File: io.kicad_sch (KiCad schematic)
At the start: 6 parts, among them J1 SM03B-SRSS-TB

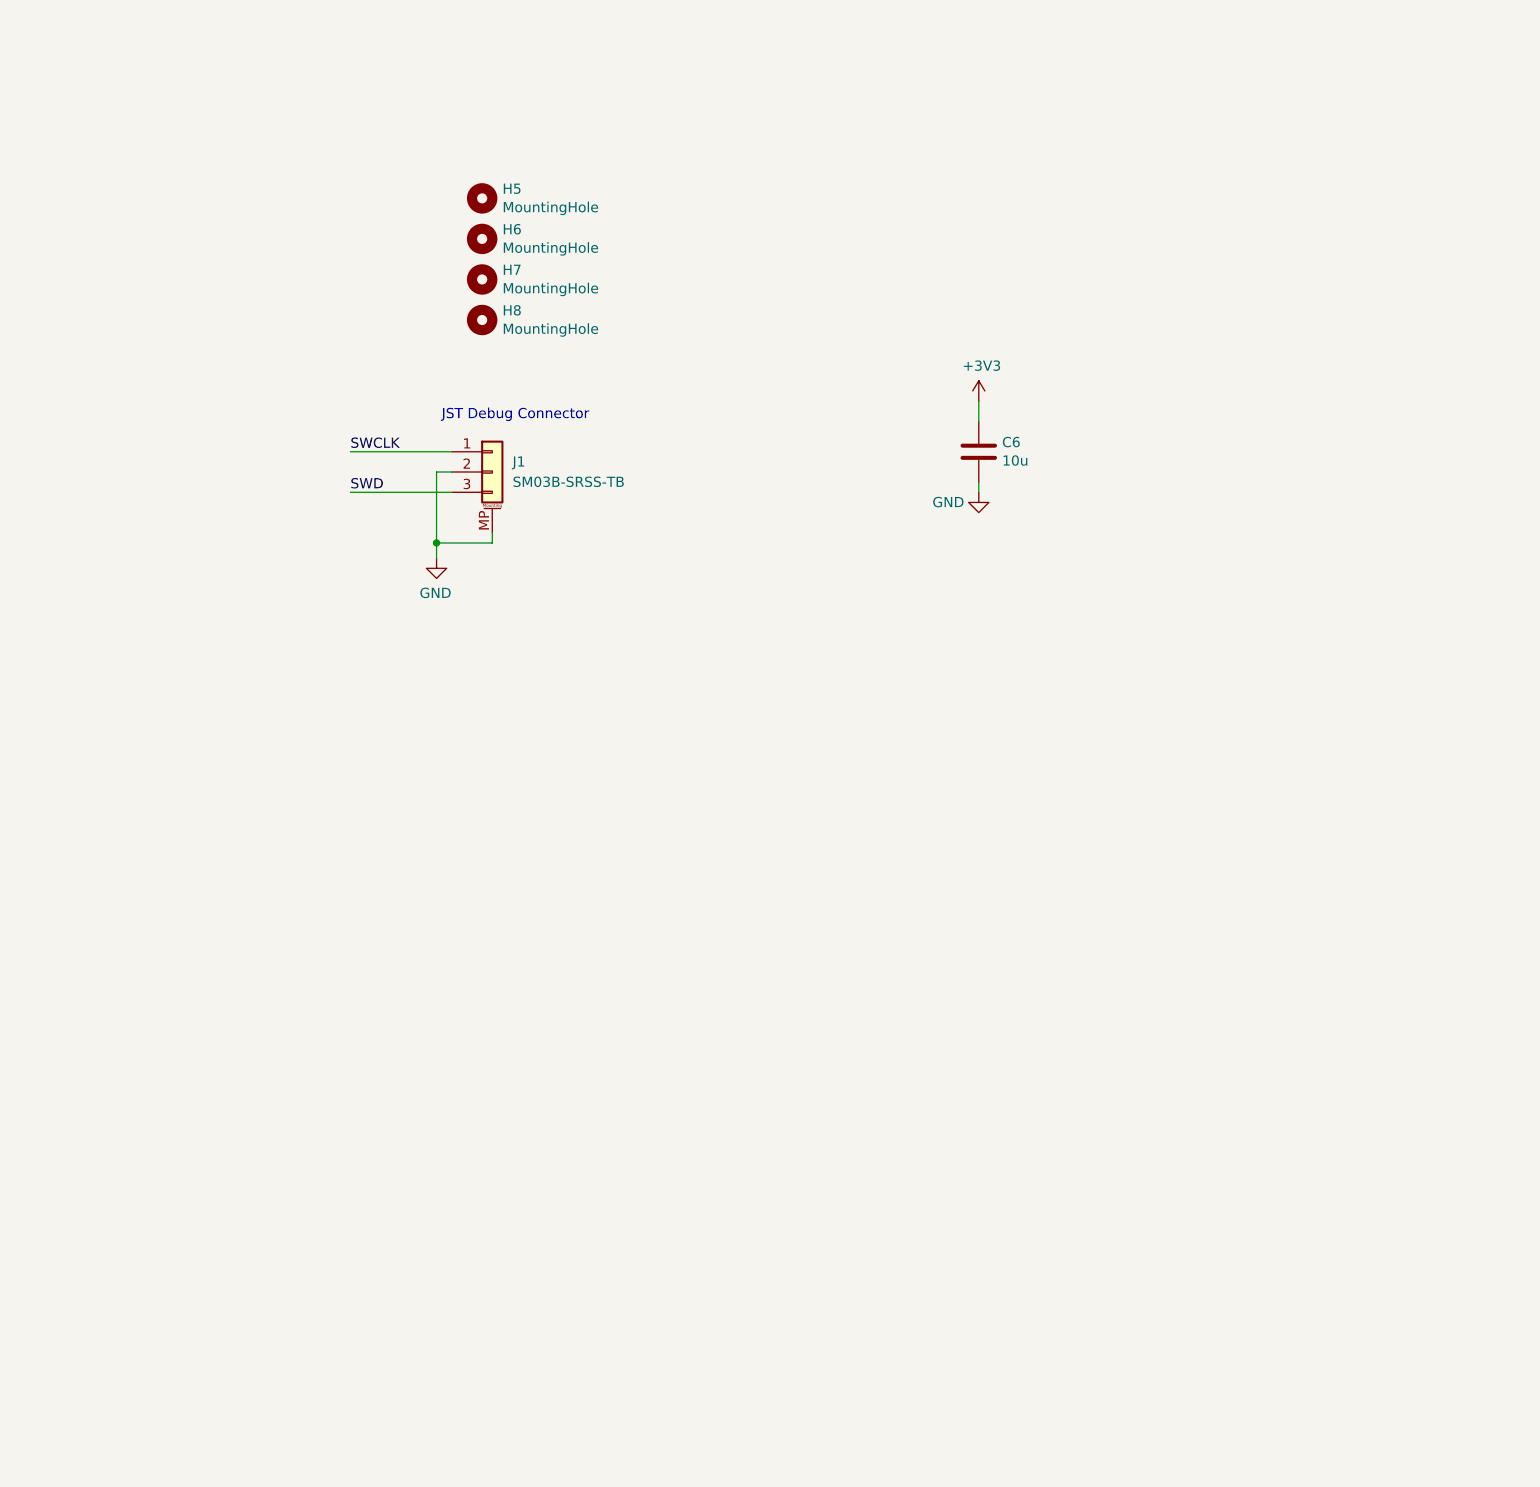
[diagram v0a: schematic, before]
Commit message: add subsheets
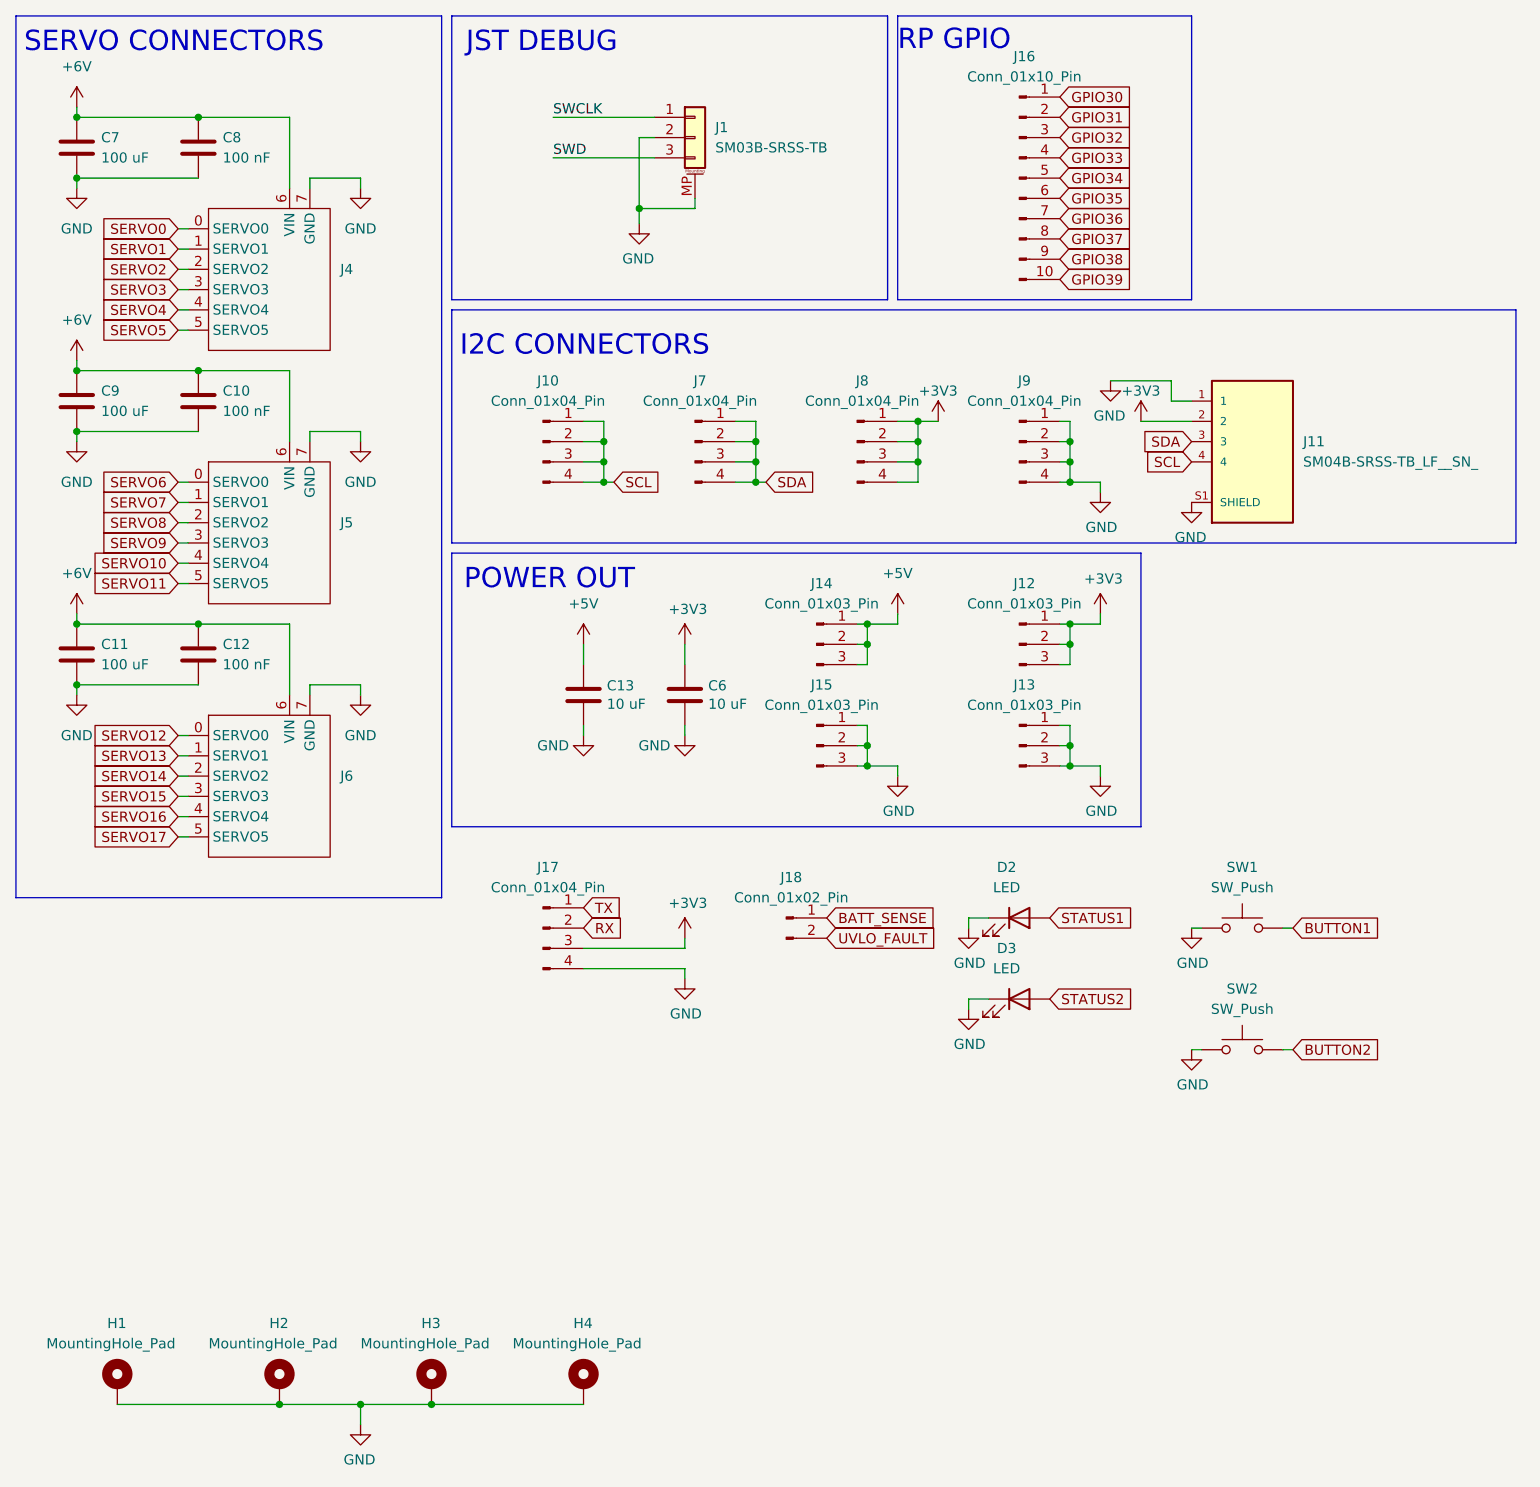
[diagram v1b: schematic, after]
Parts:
- removed H5, H6, H7, H8: MountingHole, MountingHole:MountingHole_2.7mm_M2.5, symbol Mechanical:MountingHole
- added C10, C12, C8: 100 nF, symbol Device:C
- added C11: 100 uF, Capacitor_THT:C_Radial_D5.0mm_H11.0mm_P2.00mm, symbol Device:C
- added C13: 10 uF, Capacitor_SMD:C_0805_2012Metric, symbol Device:C
- added C7, C9: 100 uF, symbol Device:C
- added D2, D3: LED, symbol Device:LED
- added H1, H2, H3, H4: MountingHole_Pad, MountingHole:MountingHole_3.2mm_M3_Pad, symbol Mechanical:MountingHole_Pad
- added J10, J17, J7, J8, J9: Conn_01x04_Pin, symbol Connector:Conn_01x04_Pin
- added J11: SM04B-SRSS-TB_LF__SN_, SM04B-SRSS-TB_LF__SN_:JST_SM04B-SRSS-TB_LF__SN_, symbol SM04B-SRSS-TB_LF__SN_:SM04B-SRSS-TB_LF__SN_
- added J12, J13, J14, J15: Conn_01x03_Pin, symbol Connector:Conn_01x03_Pin
- added J16: Conn_01x10_Pin, symbol Connector:Conn_01x10_Pin
- added J18: Conn_01x02_Pin, symbol Connector:Conn_01x02_Pin
- added J4, J5, J6: ~, symbol SC_18:Servo_3x6
- added SW1, SW2: SW_Push, symbol Switch:SW_Push
- C6: value 10u -> 10 uF
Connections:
- net +3V3: now also J11.2, J12.1 (Pin_1), J12.2 (Pin_2), J12.3 (Pin_3), J17.3 (Pin_3), J8.1 (Pin_1), J8.2 (Pin_2), J8.3 (Pin_3), J8.4 (Pin_4)
- net GND: now also C10.2, C11.2, C12.2, C13.2, C7.2, C8.2, C9.2, D2.1 (K), D3.1 (K), H1.1, H2.1, H3.1, H4.1, J11.1, J11.S1 (SHIELD), J11.S2 (SHIELD), J13.1 (Pin_1), J13.2 (Pin_2), J13.3 (Pin_3), J15.1 (Pin_1), J15.2 (Pin_2), J15.3 (Pin_3), J17.4 (Pin_4), J4.7 (GND), J5.7 (GND), J6.7 (GND), J9.1 (Pin_1), J9.2 (Pin_2), J9.3 (Pin_3), J9.4 (Pin_4), SW1.1, SW2.1
- new net +5V: C13.1, J14.1 (Pin_1), J14.2 (Pin_2), J14.3 (Pin_3)
- new net +6V: C10.1, C11.1, C12.1, C7.1, C8.1, C9.1, J4.6 (VIN), J5.6 (VIN), J6.6 (VIN)
- new net BATT_SENSE: J18.1 (Pin_1)
- new net BUTTON1: SW1.2
- new net BUTTON2: SW2.2
- new net GPIO30: J16.1 (Pin_1)
- new net GPIO31: J16.2 (Pin_2)
- new net GPIO32: J16.3 (Pin_3)
- new net GPIO33: J16.4 (Pin_4)
- new net GPIO34: J16.5 (Pin_5)
- new net GPIO35: J16.6 (Pin_6)
- new net GPIO36: J16.7 (Pin_7)
- new net GPIO37: J16.8 (Pin_8)
- new net GPIO38: J16.9 (Pin_9)
- new net GPIO39: J16.10 (Pin_10)
- new net RX: J17.2 (Pin_2)
- new net SCL: J10.1 (Pin_1), J10.2 (Pin_2), J10.3 (Pin_3), J10.4 (Pin_4), J11.4
- new net SDA: J11.3, J7.1 (Pin_1), J7.2 (Pin_2), J7.3 (Pin_3), J7.4 (Pin_4)
- new net SERVO0: J4.0 (SERVO0)
- new net SERVO1: J4.1 (SERVO1)
- new net SERVO10: J5.4 (SERVO4)
- new net SERVO11: J5.5 (SERVO5)
- new net SERVO12: J6.0 (SERVO0)
- new net SERVO13: J6.1 (SERVO1)
- new net SERVO14: J6.2 (SERVO2)
- new net SERVO15: J6.3 (SERVO3)
- new net SERVO16: J6.4 (SERVO4)
- new net SERVO17: J6.5 (SERVO5)
- new net SERVO2: J4.2 (SERVO2)
- new net SERVO3: J4.3 (SERVO3)
- new net SERVO4: J4.4 (SERVO4)
- new net SERVO5: J4.5 (SERVO5)
- new net SERVO6: J5.0 (SERVO0)
- new net SERVO7: J5.1 (SERVO1)
- new net SERVO8: J5.2 (SERVO2)
- new net SERVO9: J5.3 (SERVO3)
- new net STATUS1: D2.2 (A)
- new net STATUS2: D3.2 (A)
- new net TX: J17.1 (Pin_1)
- new net UVLO_FAULT: J18.2 (Pin_2)
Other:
- note added: "I2C CONNECTORS"
- note added: "JST DEBUG"
- note added: "POWER OUT"
- note added: "RP GPIO"
- note added: "SERVO CONNECTORS"
- note removed: "JST Debug Connector"
- moved on the sheet: C6, J1

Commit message: HELO
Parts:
- C10, C12, C8: footprint (none) -> Capacitor_SMD:C_0402_1005Metric
- C11: footprint Capacitor_THT:C_Radial_D5.0mm_H11.0mm_P2.00mm -> Capacitor_THT:CP_Radial_D5.0mm_P2.00mm
- C7, C9: footprint (none) -> Capacitor_THT:CP_Radial_D5.0mm_P2.00mm
- D2, D3: footprint (none) -> LED_SMD:LED_1206_3216Metric
- J10, J17, J7, J8, J9: footprint (none) -> Connector_PinHeader_2.54mm:PinHeader_1x04_P2.54mm_Vertical
- J12, J13, J14, J15: footprint (none) -> Connector_PinHeader_2.54mm:PinHeader_1x03_P2.54mm_Vertical
- J16: footprint (none) -> Connector_PinHeader_2.54mm:PinHeader_1x10_P2.54mm_Vertical
- J18: footprint (none) -> Connector_PinHeader_2.54mm:PinHeader_1x02_P2.54mm_Vertical
- SW1, SW2: footprint (none) -> Button_Switch_SMD:SW_Push_1P1T_NO_Vertical_Wuerth_434133025816
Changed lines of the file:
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@@
 			)
 		)
-		(property "Footprint" ""
+		(property "Footprint" "LED_SMD:LED_1206_3216Metric"
 			(at 138.43 135.89 0)
 			(effects
@@
 			)
 		)
-		(property "Footprint" ""
+		(property "Footprint" "Connector_PinHeader_2.54mm:PinHeader_1x04_P2.54mm_Vertical"
 			(at 138.43 66.04 0)
 			(effects
@@
 			)
 		)
-		(property "Footprint" ""
+		(property "Footprint" "Connector_PinHeader_2.54mm:PinHeader_1x04_P2.54mm_Vertical"
 			(at 97.79 66.04 0)
 			(effects
@@
 			)
 		)
-		(property "Footprint" ""
+		(property "Footprint" "Connector_PinHeader_2.54mm:PinHeader_1x03_P2.54mm_Vertical"
 			(at 113.03 91.44 0)
 			(effects
@@
 			)
 		)
-		(property "Footprint" ""
+		(property "Footprint" "Connector_PinHeader_2.54mm:PinHeader_1x04_P2.54mm_Vertical"
 			(at 118.11 66.04 0)
 			(effects
@@
 			)
 		)
-		(property "Footprint" ""
+		(property "Footprint" "Capacitor_SMD:C_0402_1005Metric"
 			(at 36.5252 33.02 0)
 			(effects
@@
 			)
 		)
-		(property "Footprint" ""
+		(property "Footprint" "Connector_PinHeader_2.54mm:PinHeader_1x10_P2.54mm_Vertical"
 			(at 138.43 33.02 0)
 			(effects
@@
 			)
 		)
-		(property "Footprint" ""
+		(property "Footprint" "Connector_PinHeader_2.54mm:PinHeader_1x03_P2.54mm_Vertical"
 			(at 138.43 104.14 0)
 			(effects
@@
 			)
 		)
-		(property "Footprint" ""
+		(property "Footprint" "Capacitor_THT:CP_Radial_D5.0mm_P2.00mm"
 			(at 21.2852 33.02 0)
 			(effects
@@
 			)
 		)
-		(property "Footprint" ""
+		(property "Footprint" "Connector_PinHeader_2.54mm:PinHeader_1x04_P2.54mm_Vertical"
 			(at 78.74 127 0)
 			(effects
@@
 			)
 		)
-		(property "Footprint" ""
+		(property "Footprint" "Capacitor_THT:CP_Radial_D5.0mm_P2.00mm"
 			(at 21.2852 64.77 0)
 			(effects
@@
 			)
 		)
-		(property "Footprint" "Capacitor_THT:C_Radial_D5.0mm_H11.0mm_P2.00mm"
+		(property "Footprint" "Capacitor_THT:CP_Radial_D5.0mm_P2.00mm"
 			(at 21.2852 96.52 0)
 			(effects
@@
 			)
 		)
-		(property "Footprint" ""
+		(property "Footprint" "Capacitor_SMD:C_0402_1005Metric"
 			(at 36.5252 64.77 0)
 			(effects
@@
 			)
 		)
-		(property "Footprint" ""
+		(property "Footprint" "Connector_PinHeader_2.54mm:PinHeader_1x03_P2.54mm_Vertical"
 			(at 113.03 104.14 0)
 			(effects
@@
 			)
 		)
-		(property "Footprint" ""
+		(property "Footprint" "Connector_PinHeader_2.54mm:PinHeader_1x03_P2.54mm_Vertical"
 			(at 138.43 91.44 0)
 			(effects
@@
 			)
 		)
-		(property "Footprint" ""
+		(property "Footprint" "Connector_PinHeader_2.54mm:PinHeader_1x02_P2.54mm_Vertical"
 			(at 109.22 125.73 0)
 			(effects
@@
 			)
 		)
-		(property "Footprint" ""
+		(property "Footprint" "LED_SMD:LED_1206_3216Metric"
 			(at 138.43 125.73 0)
 			(effects
@@
 			)
 		)
-		(property "Footprint" ""
+		(property "Footprint" "Connector_PinHeader_2.54mm:PinHeader_1x04_P2.54mm_Vertical"
 			(at 78.74 66.04 0)
 			(effects
@@
 			)
 		)
-		(property "Footprint" ""
+		(property "Footprint" "Button_Switch_SMD:SW_Push_1P1T_NO_Vertical_Wuerth_434133025816"
 			(at 166.37 137.16 0)
 			(effects
@@
 			)
 		)
-		(property "Footprint" ""
+		(property "Footprint" "Capacitor_SMD:C_0402_1005Metric"
 			(at 36.5252 96.52 0)
 			(effects
@@
 			)
 		)
-		(property "Footprint" ""
+		(property "Footprint" "Button_Switch_SMD:SW_Push_1P1T_NO_Vertical_Wuerth_434133025816"
 			(at 166.37 121.92 0)
 			(effects
